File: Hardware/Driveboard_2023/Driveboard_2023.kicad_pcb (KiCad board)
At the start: 2 copper layers, 122.6 x 92.7 mm, 81 parts, among them J1 6P6C, J2 RJ45_LED_Shielded, SW1 SW_Push, SW2 SW_Push, SW3 SW_Push, SW4 SW_Push, SW5 SW_Push, SW6 SW_Push, SW7 SW_SPDT, U1 Teensy4.1_DEV-16771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

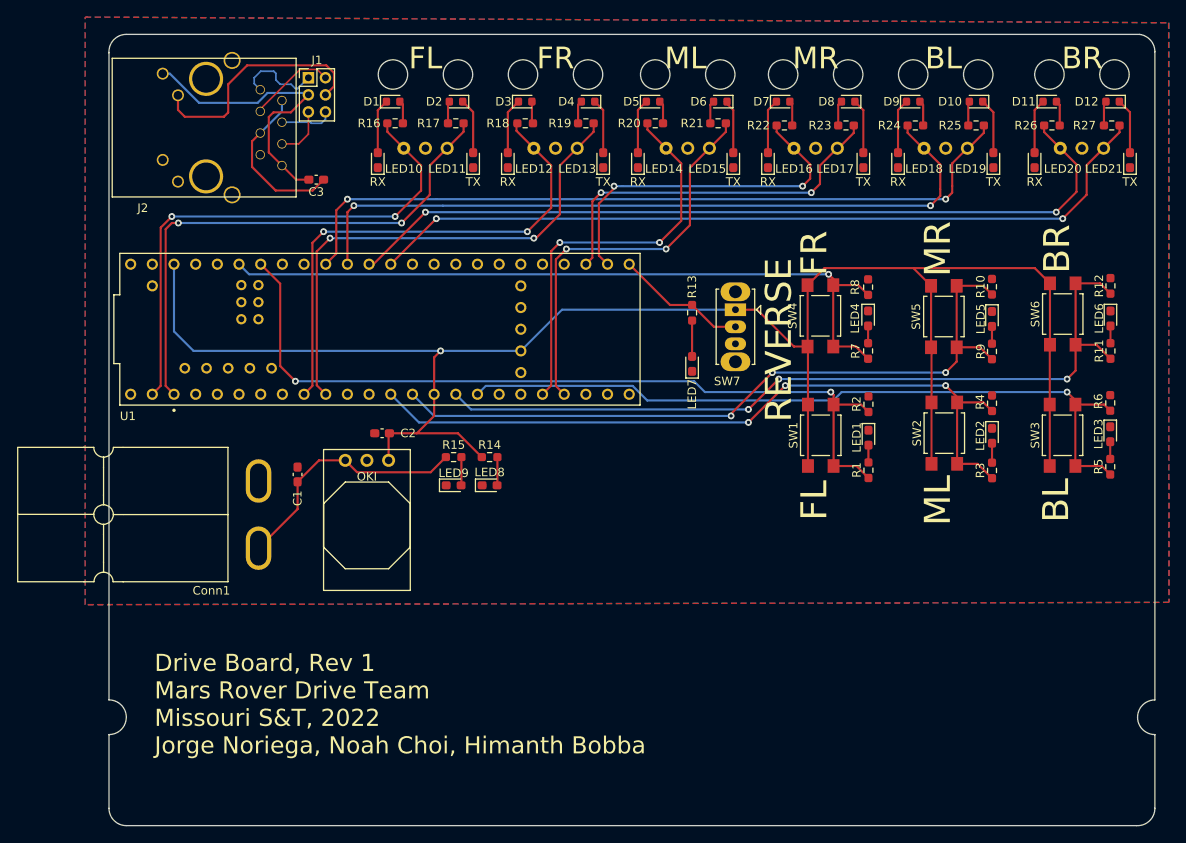
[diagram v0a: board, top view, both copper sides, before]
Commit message: Layout Review Changes
Fixed the diode's footprints
Labeled many components on PCB
Changed some traces
Added Signature
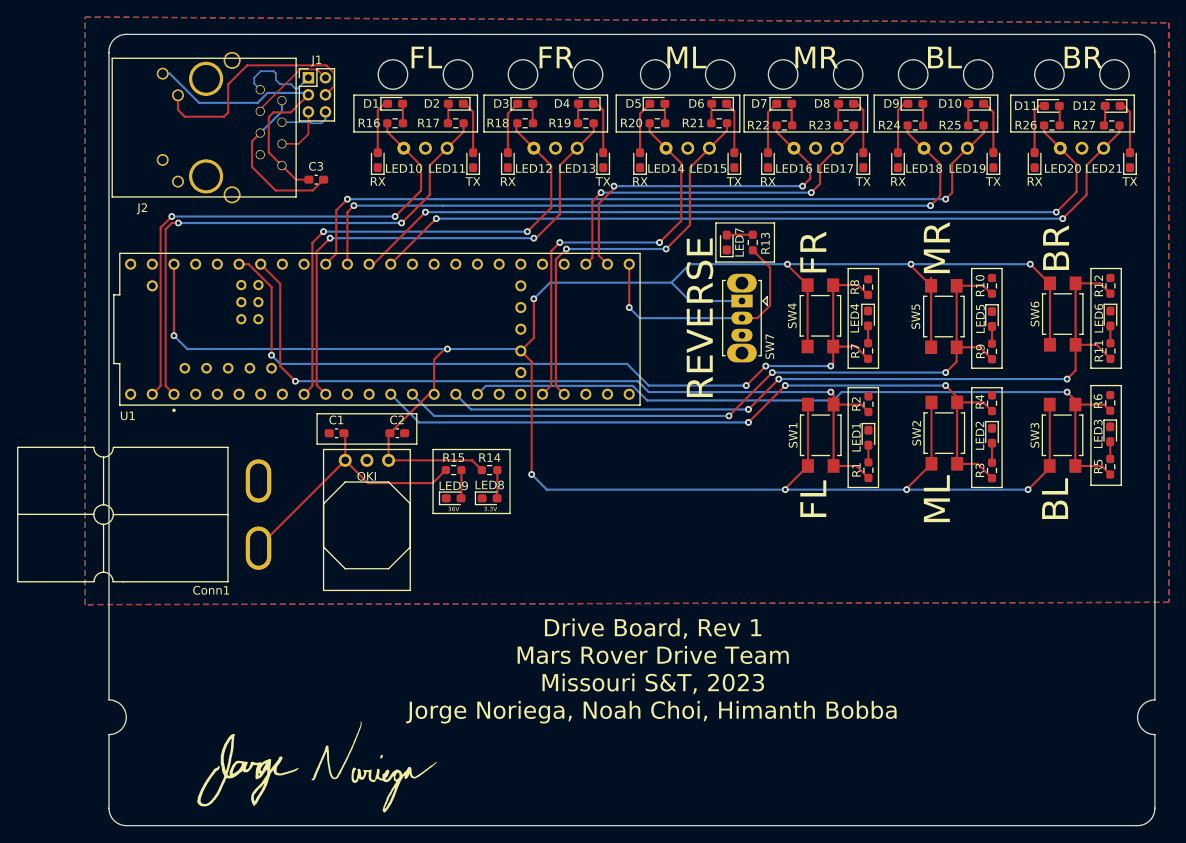
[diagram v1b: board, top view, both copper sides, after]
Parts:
- added G***: LOGO, Signatures:z_sig_Jorge_Noriega_30.0mmx13.2.0mm, F.Cu at (156.2, 122.8)
- added G***: LOGO, MRDT_Silkscreens:0_MRDT_Logo_60mm, B.Cu at (214.9, 90.9)
- D1, D10, D11, D12, D2, D3, D4, D5, D6, D7, D8, D9: footprint Diode_SMD:D_0603_1608Metric -> Diode_SMD:D_0603_1608Metric_Pad1.05x0.95mm_HandSolder
- moved LED7 14.8 mm to (204.7, 60.7)
- moved R13 10.9 mm to (207.8, 60.7), turned to -90 degrees
- moved C1 6.65 mm to (159.0, 83.1), turned to 180 degrees
- moved C2 1.78 mm to (166.1, 83.1), turned to 0 degrees
- moved LED8 1.52 mm to (176.9, 90.7)
- moved LED9 1.52 mm to (172.7, 90.7)
- moved R14 1.52 mm to (176.9, 87.4)
- moved R15 1.52 mm to (172.7, 87.4)
- moved SW7 1.27 mm to (206.5, 67.6)
- moved D5 0.57 mm to (196.6, 44.5)
- moved D11 0.57 mm to (242.8, 44.7)
- moved D12 0.51 mm to (249.9, 44.7)
- moved D8 0.36 mm to (218.7, 44.5)
- moved D4 0.36 mm to (188.2, 44.5)
- moved D9 0.36 mm to (226.8, 44.5)
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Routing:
- net +3V3: track 209.7 -> 294.7 mm, vias 1 -> 10
- net REVERSE_DIR: track 15.5 -> 30.0 mm, vias 0 -> 1
- net FR_DRIVE: track 87.5 -> 99.7 mm, vias 1 -> 4
- net +36V: track 29.4 -> 31.3 mm
- net Net-(LED7-Pad2): track 4.21 -> 3.06 mm
- net Net-(D12-Pad2): track 2.92 -> 2.34 mm
- net Net-(D8-Pad2): track 2.95 -> 2.41 mm
- net Net-(D11-Pad2): track 2.95 -> 2.41 mm
- net Net-(D9-Pad2): track 2.95 -> 2.41 mm
- net Net-(D6-Pad2): track 2.87 -> 2.34 mm
- net Net-(D4-Pad2): track 2.70 -> 2.16 mm
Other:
- board text added: "3.3V"
- board text added: "36V"
- board text added: "Drive Board, Rev 1 Mars Rover Drive Team Missouri S&T, 2023 Jorge Noriega, Noah Choi, Himanth Bobba"
- board text removed: "Drive Board, Rev 1 Mars Rover Drive Team Missouri S&T, 2022 Jorge Noriega, Noah Choi, Himanth Bobba"

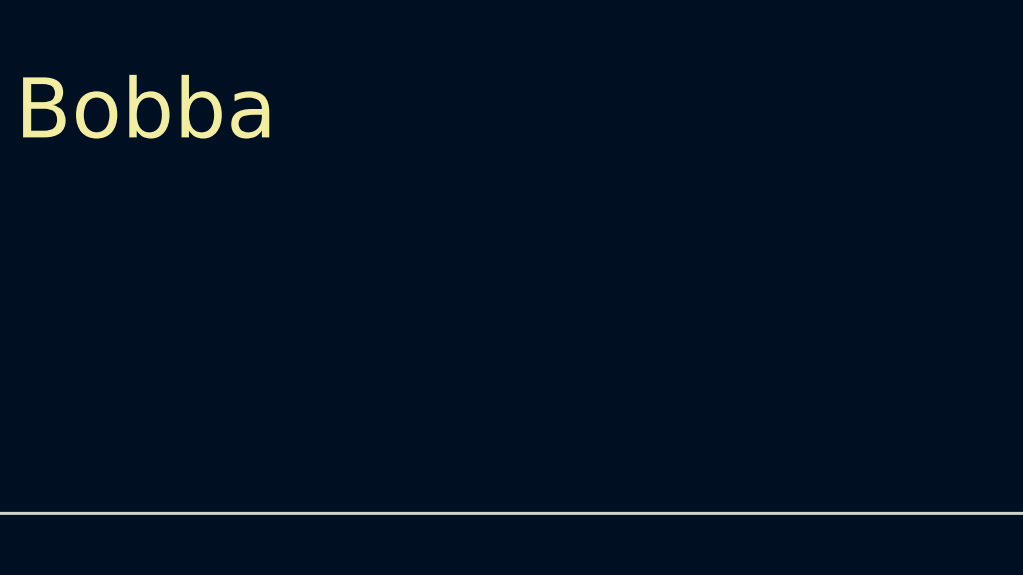
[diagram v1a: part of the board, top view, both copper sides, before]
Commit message: Signature adding and typo correction
Added my signature and corrected a typo on the board
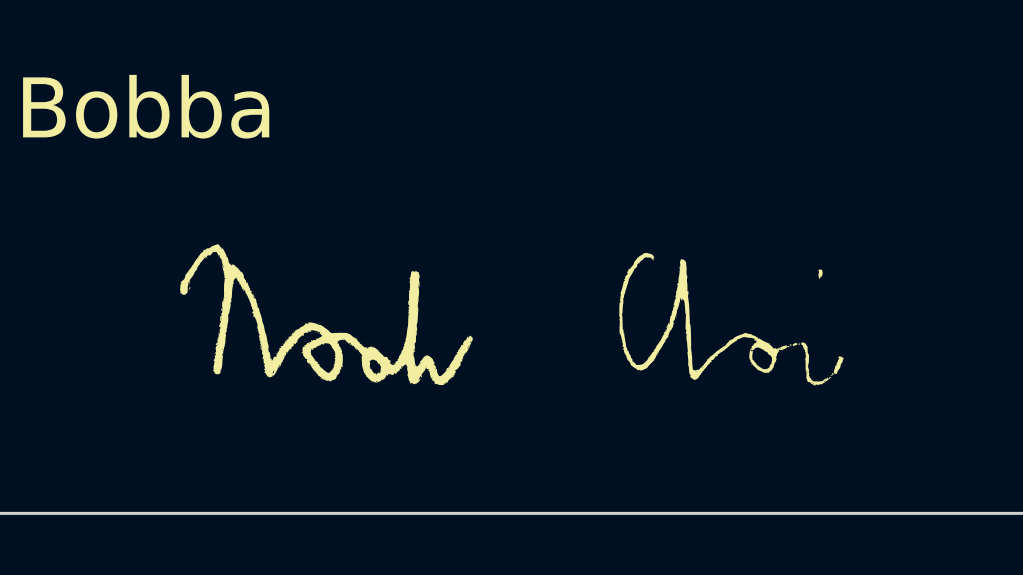
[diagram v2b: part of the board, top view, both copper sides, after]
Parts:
- added G***: LOGO, signature noah, F.Cu at (234.9, 120.7)

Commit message: Himanth Bobba Signature Added
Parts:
- added G***: LOGO, Signatures:Himanth_Bobba, F.Cu at (196.2, 122.6)

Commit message: Cleaned up board
Corrected a typo and aligned some texts boxes
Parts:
- moved G*** 12.3 mm to (219.3, 79.5)
- moved G*** 3.32 mm to (159.5, 123.2)
- moved G*** 2.27 mm to (198.5, 122.4)
- moved G*** 2.20 mm to (233.0, 119.6)
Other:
- board text added: "Drive Board, Rev 1 Mars Rover Design Team Missouri S&T, 2023 Jorge Noriega, Himanth Bobba, Noah Choi"
- board text removed: "Drive Board, Rev 1 Mars Rover Drive Team Missouri S&T, 2023 Jorge Noriega, Noah Choi, Himanth Bobba"
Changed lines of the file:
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@@
   )
   (footprint "signature noah" (layer "F.Cu")
-    (at 234.95 120.65)
+    (at 232.998169 119.642586)
     (attr board_only exclude_from_pos_files exclude_from_bom)
     (fp_text reference "G***" (at 0 0) (layer "F.SilkS") hide
@@
   )
   (footprint "Signatures:z_sig_Jorge_Noriega_30.0mmx13.2.0mm" (layer "F.Cu")
-    (at 156.237137 122.795345)
+    (at 159.539137 123.176345)
     (attr board_only exclude_from_pos_files exclude_from_bom)
     (fp_text reference "G***" (at 0 0) (layer "F.SilkS") hide
@@
   )
   (footprint "Signatures:Himanth_Bobba" (layer "F.Cu")
-    (at 196.215 122.555)
+    (at 198.475207 122.386262)
     (attr board_only exclude_from_pos_files exclude_from_bom)
     (fp_text reference "G***" (at 0.033386 2.54) (layer "Dwgs.User")
@@
   )
   (footprint "MRDT_Silkscreens:0_MRDT_Logo_60mm" (layer "B.Cu")
-    (at 214.884 90.932 -90)
+    (at 219.329 79.502 -90)
     (tags "Logo, MRDT")
     (attr through_hole)
@@
     (effects (font (size 3.048 3.048) (thickness 0.15)))
   )
-  (gr_text "Drive Board, Rev 1\nMars Rover Drive Team\nMissouri S&T, 2023\nJorge Noriega, Noah Choi, Himanth Bobba" (at 196.088 110.744) (layer "F.SilkS")
+  (gr_text "Drive Board, Rev 1\nMars Rover Design Team\nMissouri S&T, 2023\nJorge Noriega, Himanth Bobba, Noah Choi" (at 196.088 110.744) (layer "F.SilkS")
     (effects (font (size 2 2) (thickness 0.15)))
   )
